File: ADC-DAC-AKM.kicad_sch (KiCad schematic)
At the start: 0 parts

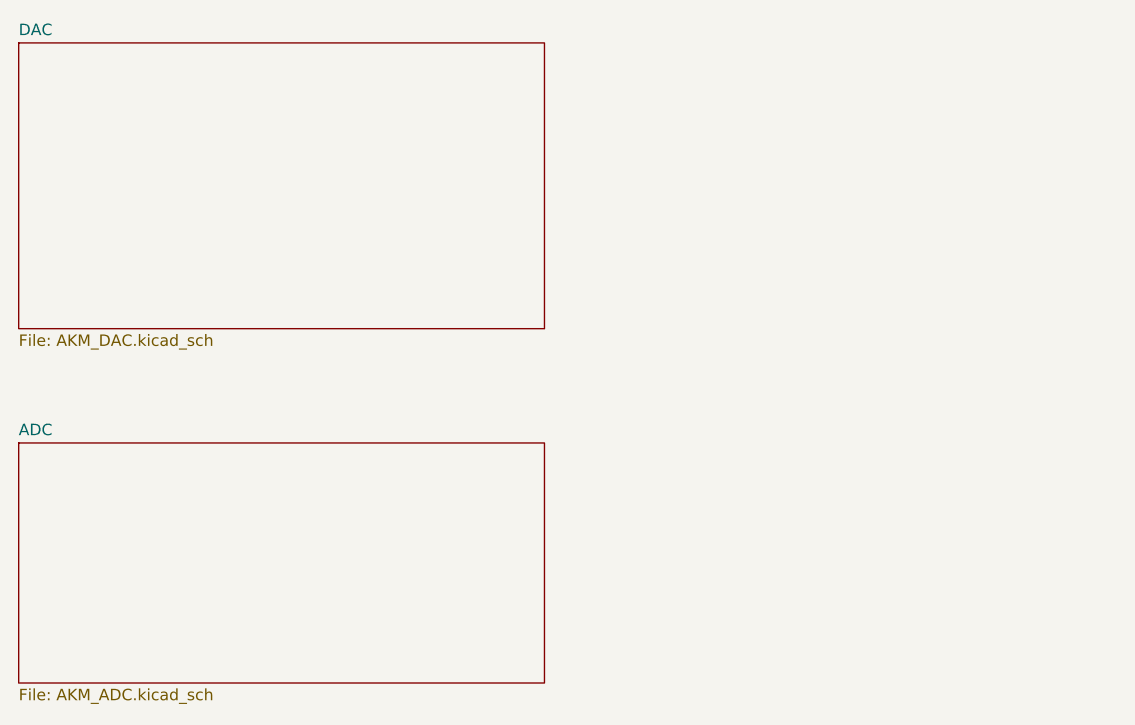
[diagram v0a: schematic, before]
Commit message: Add interfaces sheet
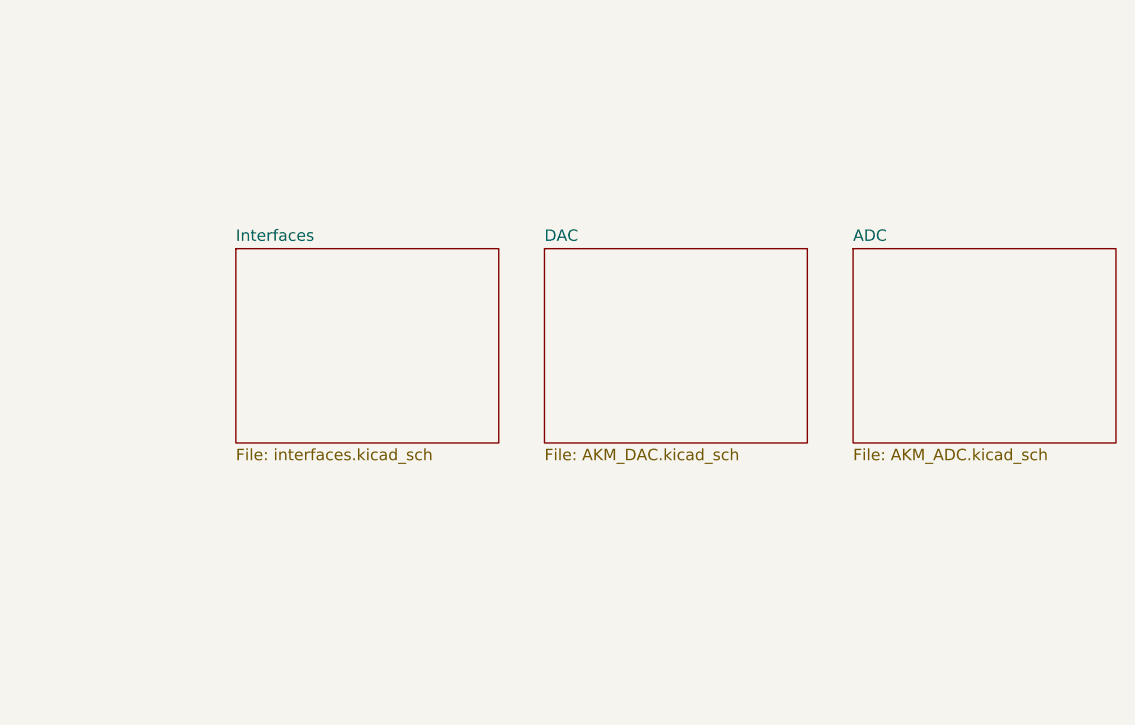
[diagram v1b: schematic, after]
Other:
- added sheet Interfaces (interfaces.kicad_sch)
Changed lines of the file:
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@@
 (kicad_sch (version 20230121) (generator eeschema)
   (paper "A5")
-  (sheet (at 30.48 69.85) (size 58.42 26.67) (fields_autoplaced)
+  (sheet (at 123.19 48.26) (size 29.21 21.59) (fields_autoplaced)
     (stroke (width 0.1524) (type solid))
     (fill (color 0 0 0 0.0000))
-    (property "Sheetname" "ADC" (at 30.48 69.1384 0)
+    (property "Sheetname" "ADC" (at 123.19 47.5484 0)
       (effects (font (size 1.27 1.27)) (justify left bottom))
     )
-    (property "Sheetfile" "AKM_ADC.kicad_sch" (at 30.48 97.1046 0)
+    (property "Sheetfile" "AKM_ADC.kicad_sch" (at 123.19 70.4346 0)
       (effects (font (size 1.27 1.27)) (justify left top))
     )
@@
     )
   )
-  (sheet (at 30.48 25.4) (size 58.42 31.75) (fields_autoplaced)
+  (sheet (at 54.61 48.26) (size 29.21 21.59) (fields_autoplaced)
     (stroke (width 0.1524) (type solid))
     (fill (color 0 0 0 0.0000))
-    (property "Sheetname" "DAC" (at 30.48 24.6884 0)
+    (property "Sheetname" "Interfaces" (at 54.61 47.5484 0)
       (effects (font (size 1.27 1.27)) (justify left bottom))
     )
-    (property "Sheetfile" "AKM_DAC.kicad_sch" (at 30.48 57.7346 0)
+    (property "Sheetfile" "interfaces.kicad_sch" (at 54.61 70.4346 0)
       (effects (font (size 1.27 1.27)) (justify left top))
     )
+    (instances
+      (project "ADC-DAC-AKM"
+        (path "/3a13adc5-7b21-4313-ae0e-90b78e0ecd25" (page "4"))
+      )
+    )
+  )
+  (sheet (at 88.9 48.26) (size 29.21 21.59) (fields_autoplaced)
+    (stroke (width 0.1524) (type solid))
+    (fill (color 0 0 0 0.0000))
+    (property "Sheetname" "DAC" (at 88.9 47.5484 0)
+      (effects (font (size 1.27 1.27)) (justify left bottom))
+    )
+    (property "Sheetfile" "AKM_DAC.kicad_sch" (at 88.9 70.4346 0)
+      (effects (font (size 1.27 1.27)) (justify left top))
+    )
